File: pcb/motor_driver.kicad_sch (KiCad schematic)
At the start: 25 parts, among them Q1 CSD19532Q5B, Q2 CSD19532Q5B, Q3 CSD19532Q5B, Q4 CSD19532Q5B, Q5 CSD19532Q5B, Q6 CSD19532Q5B, U2 DRV8353S

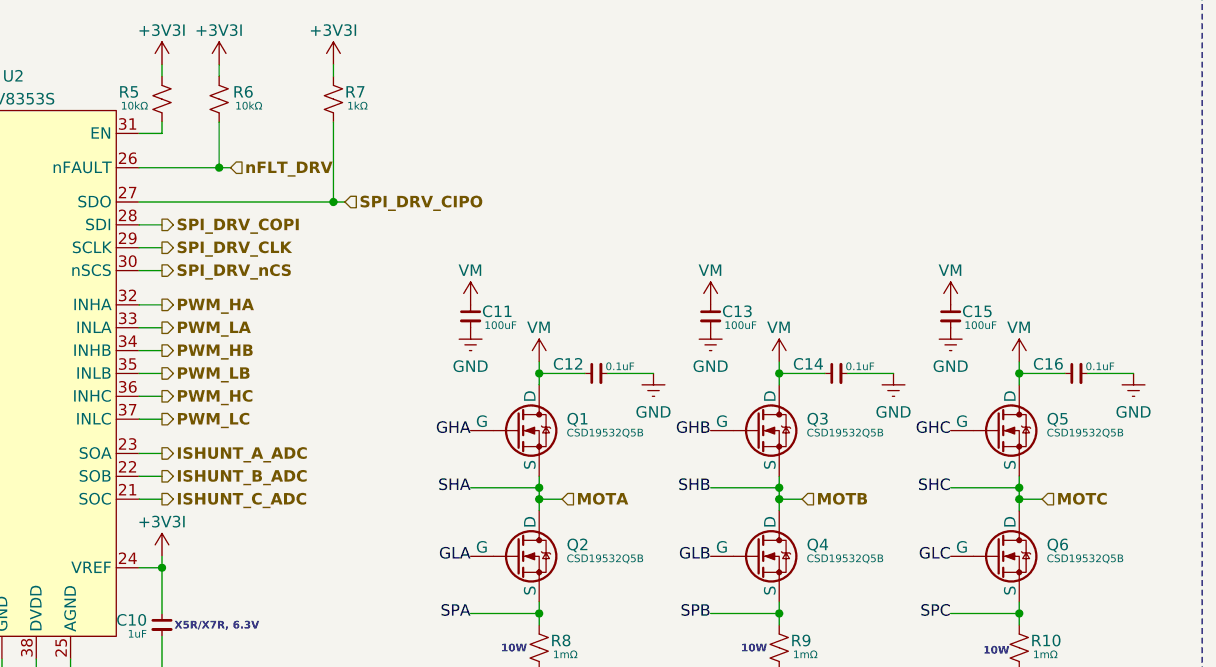
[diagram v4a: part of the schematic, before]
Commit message: Updating label direction, added more info on io
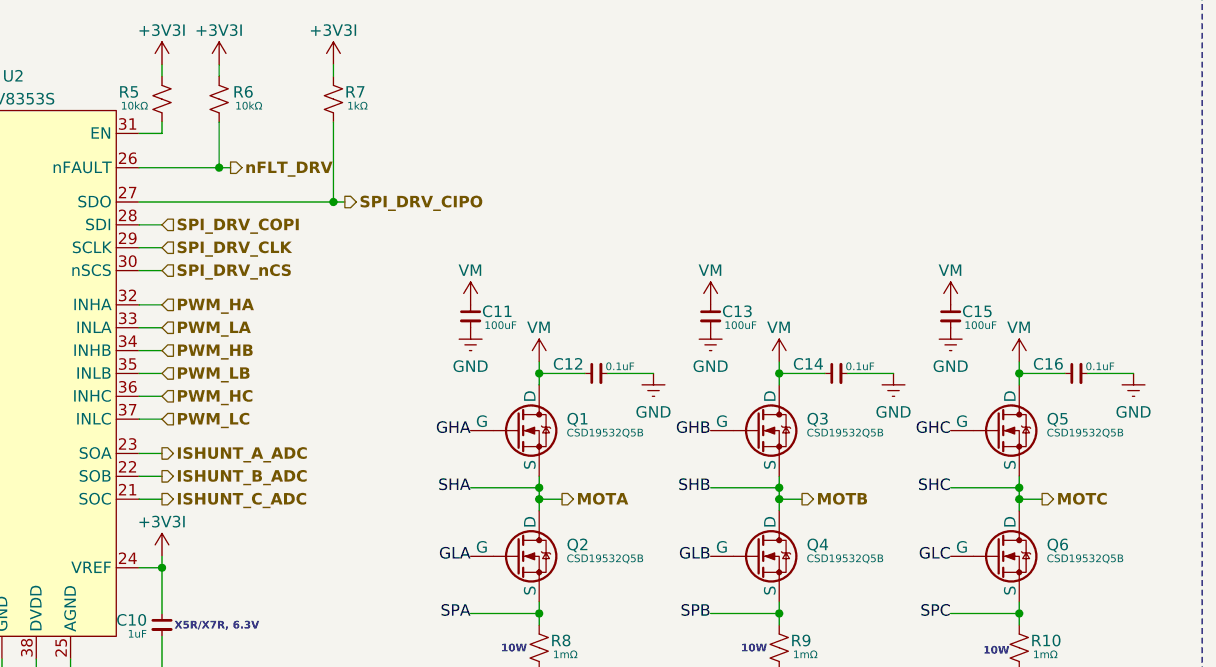
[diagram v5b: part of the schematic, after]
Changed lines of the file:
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@@
 	)
 	(hierarchical_label "nFLT_DRV"
-		(shape input)
+		(shape output)
 		(at 120.65 71.12 0)
 		(effects
@@
 	)
 	(hierarchical_label "MOTA"
-		(shape input)
+		(shape output)
 		(at 157.48 107.95 0)
 		(effects
@@
 	)
 	(hierarchical_label "PWM_LC"
-		(shape output)
+		(shape input)
 		(at 113.03 99.06 0)
 		(effects
@@
 	)
 	(hierarchical_label "PWM_HC"
-		(shape output)
+		(shape input)
 		(at 113.03 96.52 0)
 		(effects
@@
 	)
 	(hierarchical_label "SPI_DRV_CIPO"
-		(shape input)
+		(shape output)
 		(at 133.35 74.93 0)
 		(effects
@@
 	)
 	(hierarchical_label "PWM_HA"
-		(shape output)
+		(shape input)
 		(at 113.03 86.36 0)
 		(effects
@@
 	)
 	(hierarchical_label "PWM_LA"
-		(shape output)
+		(shape input)
 		(at 113.03 88.9 0)
 		(effects
@@
 	)
 	(hierarchical_label "MOTC"
-		(shape input)
+		(shape output)
 		(at 210.82 107.95 0)
 		(effects
@@
 	)
 	(hierarchical_label "PWM_LB"
-		(shape output)
+		(shape input)
 		(at 113.03 93.98 0)
 		(effects
@@
 	)
 	(hierarchical_label "SPI_DRV_nCS"
-		(shape output)
+		(shape input)
 		(at 113.03 82.55 0)
 		(effects
@@
 	)
 	(hierarchical_label "SPI_DRV_COPI"
-		(shape output)
+		(shape input)
 		(at 113.03 77.47 0)
 		(effects
@@
 	)
 	(hierarchical_label "PWM_HB"
-		(shape output)
+		(shape input)
 		(at 113.03 91.44 0)
 		(effects
@@
 	)
 	(hierarchical_label "MOTB"
-		(shape input)
+		(shape output)
 		(at 184.15 107.95 0)
 		(effects
@@
 	)
 	(hierarchical_label "SPI_DRV_CLK"
-		(shape output)
+		(shape input)
 		(at 113.03 80.01 0)
 		(effects
@@
 			)
 		)
-		(property "Datasheet" "https://www.ti.com/lit/ds/symlink/drv8353.pdf?ts=1745712501970&ref_url=https%253A%252F%252Fwww.ti.com%252Fproduct%252FDRV8353%253Fdcmp%253Ddsproject%2526hqs%253Dsupport%2526"
+		(property "Datasheet" "https://www.ti.com/lit/ds/symlink/drv8353.pdf"
 			(at 96.52 90.17 0)
 			(effects

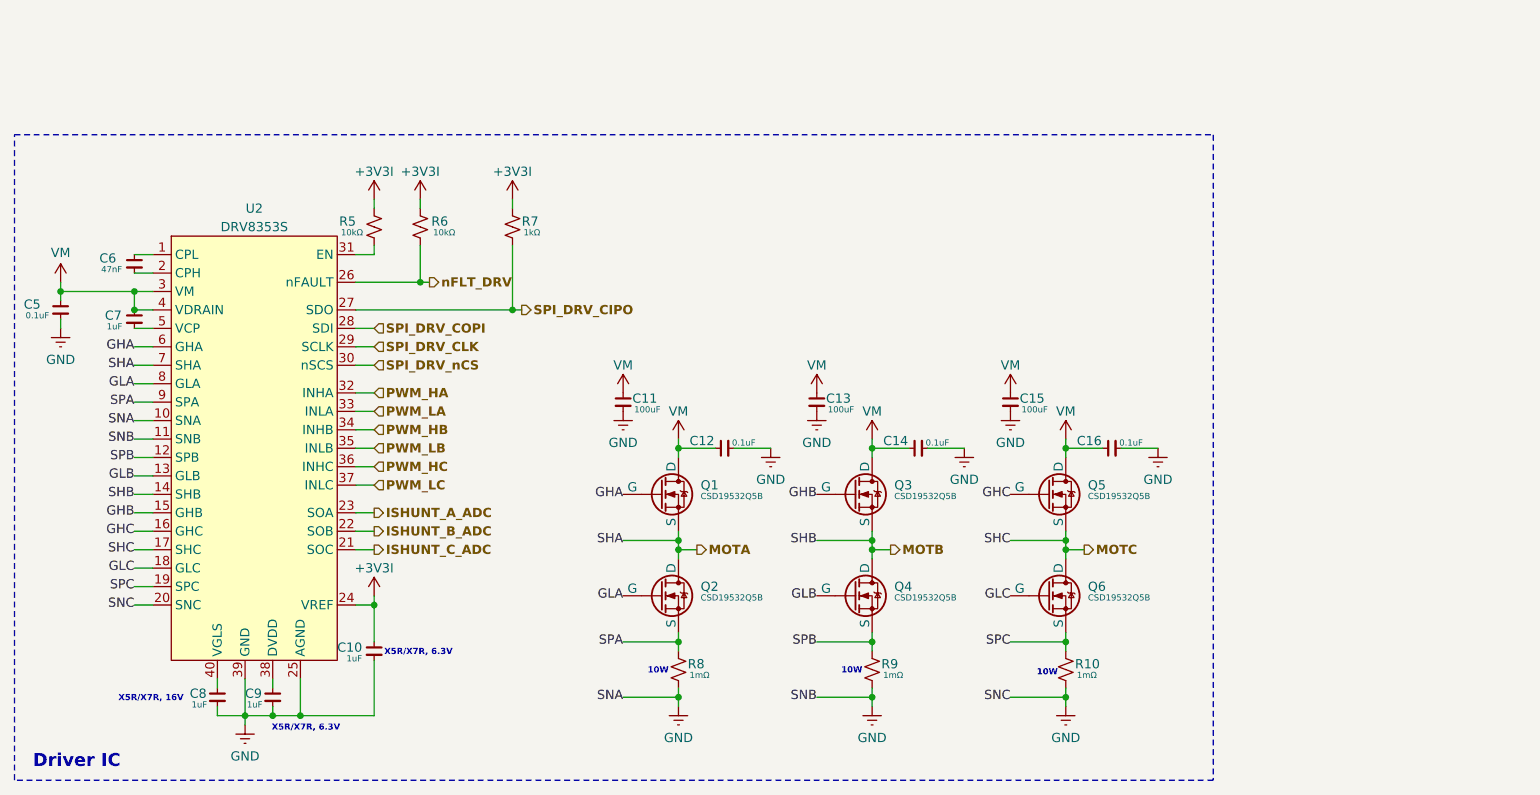
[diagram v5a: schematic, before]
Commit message: Made updates to the power and driver sheet
Fixed converters and added motor connector
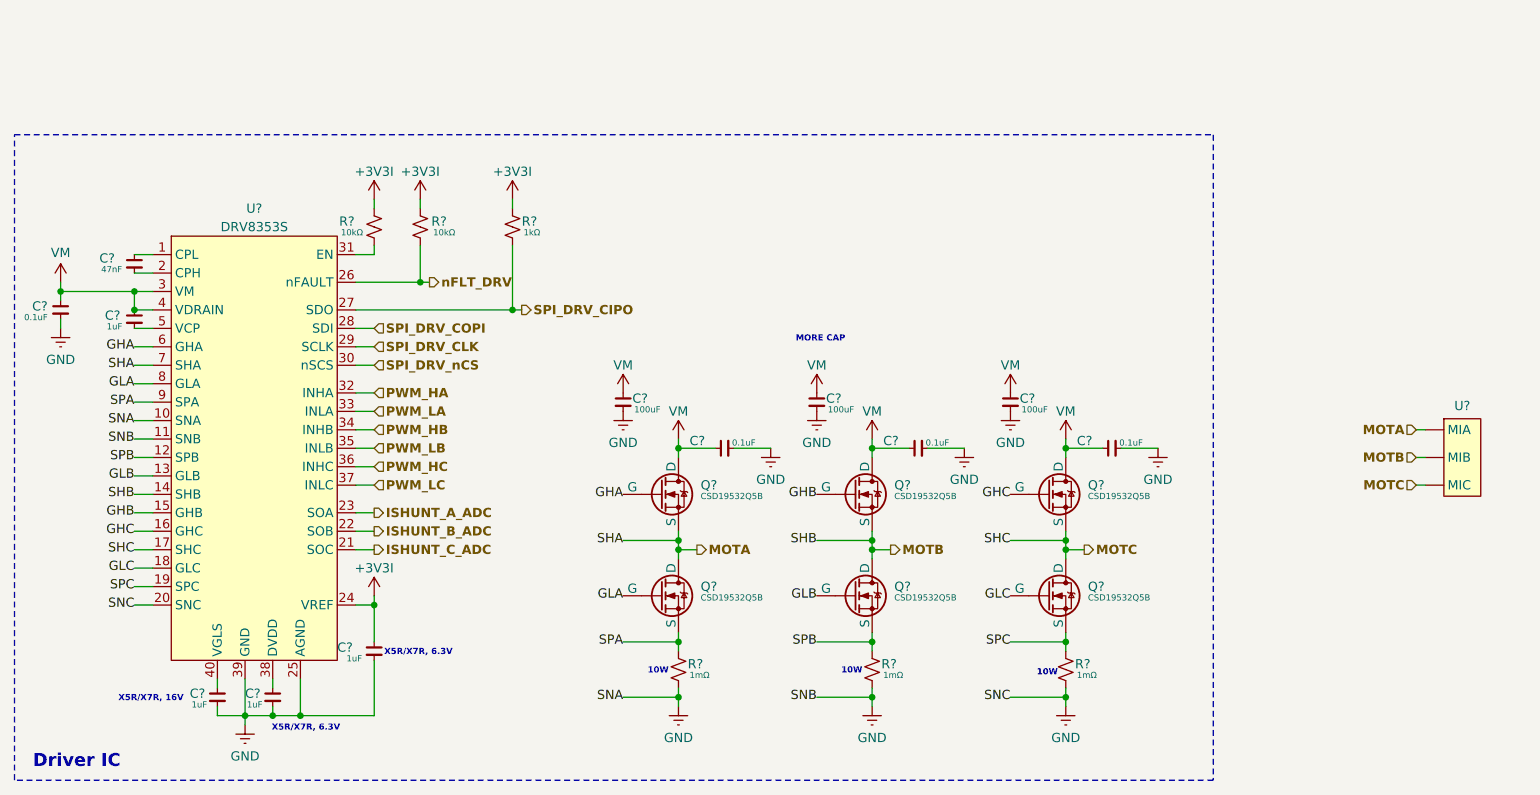
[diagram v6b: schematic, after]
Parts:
- added U?: ~, symbol Symbols:Lug_Mount_Connector
- renumbered C7 to C?, C13 to C?, C9 to C?, C8 to C?, C10 to C?, C12 to C?, C14 to C?, C11 to C?, C15 to C?, C5 to C?, C6 to C?, C16 to C?, Q3 to Q?, Q2 to Q?, Q6 to Q?, Q4 to Q?, Q5 to Q?, Q1 to Q?, R10 to R?, R9 to R?, R5 to R?, R7 to R?, R8 to R?, R6 to R?, U2 to U?
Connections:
- net MOTA: now also U?. (MIC)
- net MOTB: now also U?. (MIC)
- net MOTC: now also U?. (MIC)
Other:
- note added: "MORE CAP"

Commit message: Light review and notes
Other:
- note added: "probably powerpole"
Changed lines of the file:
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@@
+		)
+	)
+	(text "probably powerpole"
+		(exclude_from_sim no)
+		(at 260.096 104.394 0)
+		(effects
+			(font
+				(size 1.27 1.27)
+				(thickness 0.254)
+				(bold yes)
+			)
 		)
 	)
